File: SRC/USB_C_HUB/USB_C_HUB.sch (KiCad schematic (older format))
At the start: 14 parts

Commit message: commit with all DFPs properly connected
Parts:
- added C? (x6): 10uF, symbol Device:C_Small
- added C? (x3): 100nF, symbol Device:C_Small
- added R? (x3): 6.8K, symbol Device:R_US
- added U? (x3): SY6280, Package_TO_SOT_SMD:SOT-23-5, symbol usb_hub:SY6280
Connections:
- net USB3DN_RXDN1: no longer J?.B10 (RX1-)
- net at J?.A4 (VBUS), J?.A9 (VBUS), J?.B4 (VBUS)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: now also C?.1, C?.1, U?.1 (OUT)
- net at J?.1 (VBUS): now also C?.1, C?.1, U?.1 (OUT)
- net at P?.A4 (VBUS), P?.A9 (VBUS), P?.B4 (VBUS)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: now also C?.1, C?.1, U?.1 (OUT)
- new net: C?.2, C?.2, C?.2, R?.2, U?.2 (GND) (x2)
- new net: R?.1, U?.3 (ISET) (x3)
- new net: C?.1, U?.4 (EN), U?.5 (IN) (x3)
- new net: C?.2, C?.2, R?.2, U?.2 (GND)
- no-connect marks 22 -> 24
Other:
- note added: "Iset=6800/rs\n1A limit\nr2=6.8k"
- note added: "OVER CURRENT &\nSHORT CIRCUIT \nPROTETION"

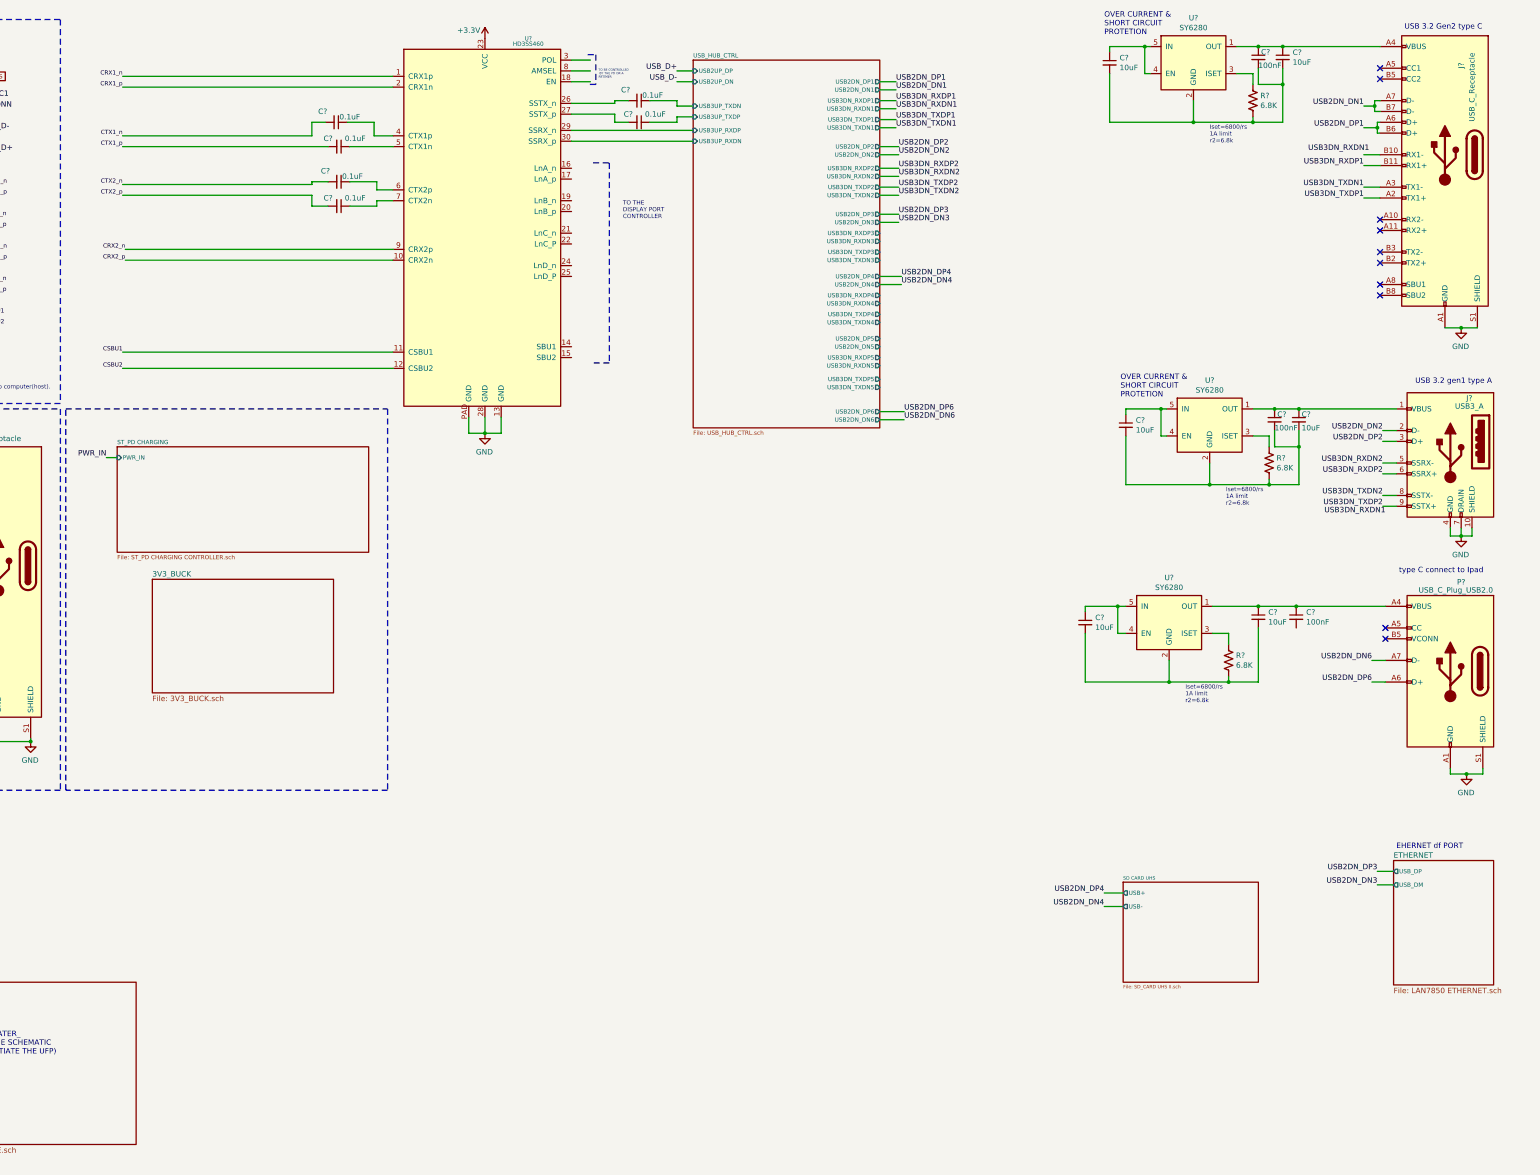
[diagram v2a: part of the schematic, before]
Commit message: all but HDMI + 2 DFP ports
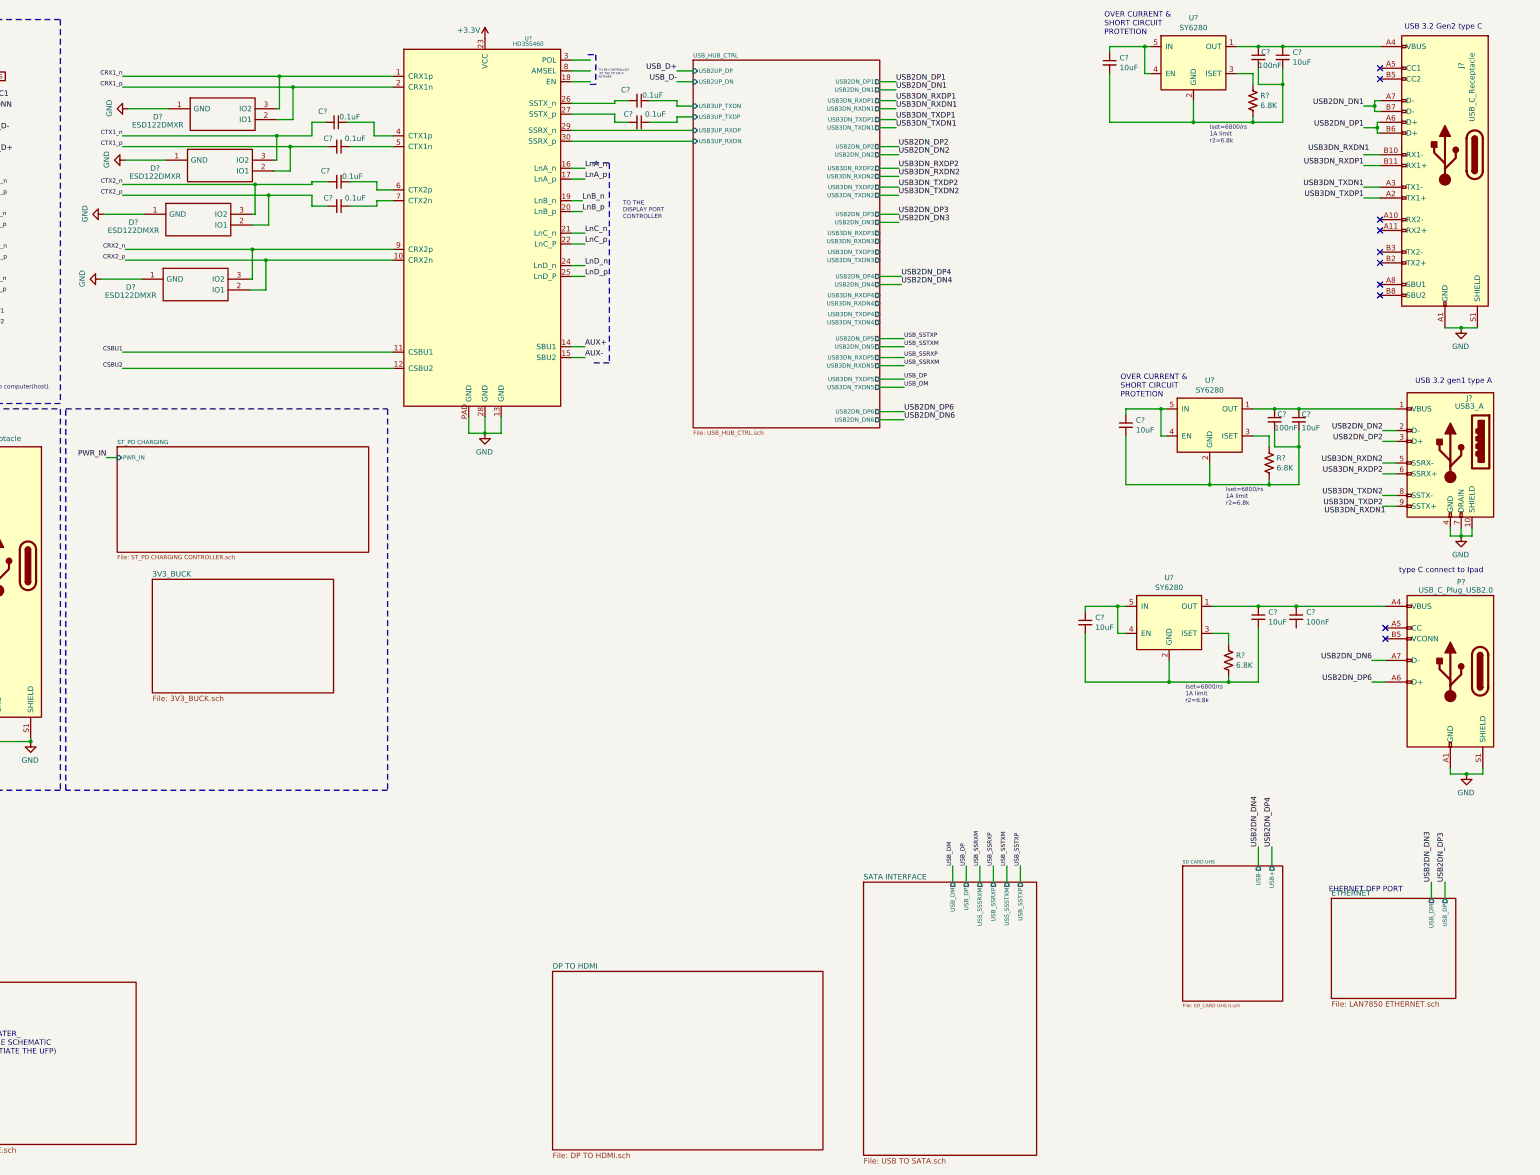
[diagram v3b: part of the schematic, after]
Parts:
- added D? (x4): ESD122DMXR, DMX0003A, symbol SamacSys_Parts:ESD122DMXR
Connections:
- net CRX1_n: now also D?.3 (IO2)
- net CRX1_p: now also D?.2 (IO1)
- net CRX2_n: now also D?.3 (IO2)
- net CRX2_p: now also D?.2 (IO1)
- net CTX1_n: now also D?.3 (IO2)
- net CTX1_p: now also D?.2 (IO1)
- net CTX2_n: now also D?.3 (IO2)
- net CTX2_p: now also D?.2 (IO1)
- net GND: now also D?.1 (GND), D?.1 (GND), D?.1 (GND), D?.1 (GND)
- net AUX+: now reaches U?.14 (SBU1)
- net AUX-: now reaches U?.15 (SBU2)
- net LnA_n: now reaches U?.16 (LnA_n)
- net LnA_p: now reaches U?.17 (LnA_p)
- net LnB_n: now reaches U?.19 (LnB_n)
- net LnB_p: now reaches U?.20 (LnB_p)
- net LnC_n: now reaches U?.21 (LnC_n)
- net LnC_p: now reaches U?.22 (LnC_P)
- net LnD_n: now reaches U?.24 (LnD_n)
- net LnD_p: now reaches U?.25 (LnD_P)
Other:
- note added: "EHERNET DFP PORT"
- note removed: "EHERNET df PORT"

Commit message: all but HDMI and UFP PD
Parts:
- added C? (x2): 10uF, symbol Device:C_Small
- added C?: 100nF, symbol Device:C_Small
- added J?: USB3_A, symbol Connector:USB3_A
- added R?: 6.8K, symbol Device:R_US
- added U?: SY6280, Package_TO_SOT_SMD:SOT-23-5, symbol usb_hub:SY6280
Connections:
- net GND: now also J?.10 (SHIELD), J?.4 (GND), J?.7 (DRAIN)
- net USB2DN_DN3: now also J?.2 (D-)
- net USB2DN_DP3: now also J?.3 (D+)
- new net: C?.1, C?.1, J?.1 (VBUS), U?.1 (OUT)
- new net: R?.1, U?.3 (ISET)
- new net: C?.2, C?.2, C?.2, R?.2, U?.2 (GND)
- new net: C?.1, U?.4 (EN), U?.5 (IN)
- new net USB3DN_RXDN3: J?.5 (SSRX-)
- new net USB3DN_RXDP3: J?.6 (SSRX+)
- new net USB3DN_TXDN3: J?.8 (SSTX-)
- new net USB3DN_TXDP3: J?.9 (SSTX+)
- no-connect marks 24 -> 28
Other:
- note added: "OUTPUT SECTIONS\n (DFP)"
- note added: "USB 3.2 gen1 type A(NO. 2)\n"
- moved on the sheet: C?, P?, R?, U?

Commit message: ALL DONE BUT THE HDMI SECTION. NEED FOOTPRINT ASSIGNMENT
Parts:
- added D1, D4: ESD122DMXR, SamacSys_Parts_2:DMX0003A, symbol SamacSys_Parts:ESD122DMXR
- added R2, R3: 1M, symbol Device:R_US
- D2, D3, D5, D6: renamed from D?; footprint DMX0003A -> SamacSys_Parts_2:DMX0003A
- gave numbers to parts that had none: 35
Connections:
- net +3V3: now also U1.18 (EN), R2.1, R3.2
- net AUX+: now also R2.2
- net AUX-: now also R3.1
- net GND: now also U1.8 (AMSEL), D1.1 (GND), D4.1 (GND)
- net USB3DN_RXDN1: now also J4.B10 (RX1-)
- net USB_D+: now also D4.3 (IO2)
- net USB_D-: now also D4.2 (IO1)
- net VCONN: now also D1.2 (IO1), D1.3 (IO2)
- net AB_OUT: now reaches U1.3 (POL)
- no-connect marks 28 -> 30
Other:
- note added: "ESD PROTECTION"
- note added: "HDMI"
- note added: "INTERFACE SECTION"
- note added: "MICRO SD"
- note added: "OUTPUT SECTION\n (DFP)"
- note added: "PD CONTROLLER INPUT\n SINK"
- note added: "POWER CONVERSION SECTION"
- note added: "POWER SECTION"
- note added: "SATA\n"
- note added: "This PD handles power negtiation with the charger\n(the power source) It advertises itself as the sink.\nRequest for 100W (20V 5A)"
- note added: "This section has a PD controller that\nAdvertizes itself as a source to the \nconnected device(UFP). It then checks the\nneeds of the Device and supplies the needed power.\n(THUS THE HUB MEETS THE USB PD STANDARDS)"
- note added: "UHS SD"
- note added: "USB C HUB EXTENSION"
- note added: "USB C HUB(HIGH SPEED)"
- note added: "USB C MUX"
- note added: "USB PD CONTROLLER\n(POWER SOURCE)"
- note removed: "OUTPUT SECTIONS\n (DFP)"
- note removed: "PRESERVED FOR USE LATER_\nNO CONNECTION TO THE SCHEMATIC\n(MAYBE NEEDED TO INITIATE THE UFP)"
- moved on the sheet: C10, C11, C13, C14, C15, C17, C18, C19, C8, J1, J2, J3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

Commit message: schematic capture complete. Pending Footprint assignment. accetable Errors=21
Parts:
- added D14: ESD122DMXR, SamacSys_Parts_2:DMX0003A, symbol SamacSys_Parts:ESD122DMXR
- renumbered C16 to C15, C15 to C16
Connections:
- net GND: now also D14.1 (GND)
- net USB2DN_DN6: now also D14.2 (IO1)
- net USB2DN_DP6: now also D14.3 (IO2)
- net +5V: now reaches C9.1, U3.4 (EN), U3.5 (IN)
- net +5V: now also C10.1, C11.1, C8.1, U2.4 (EN), U2.5 (IN), U4.4 (EN), U4.5 (IN), U5.4 (EN), U5.5 (IN)
- net at C13.2, C8.2, R4.2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: now also C18.2
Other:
- moved on the sheet: C10, C11, C12, C13, C14, C15, C16, C17, C18, C19, C2, C3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
